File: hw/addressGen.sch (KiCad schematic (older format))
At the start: 6 parts, among them U103 74ACT283, U104 74ACT283, U105 74ACT283, U106 74ACT283, U107 74HC574, U108 74HC574

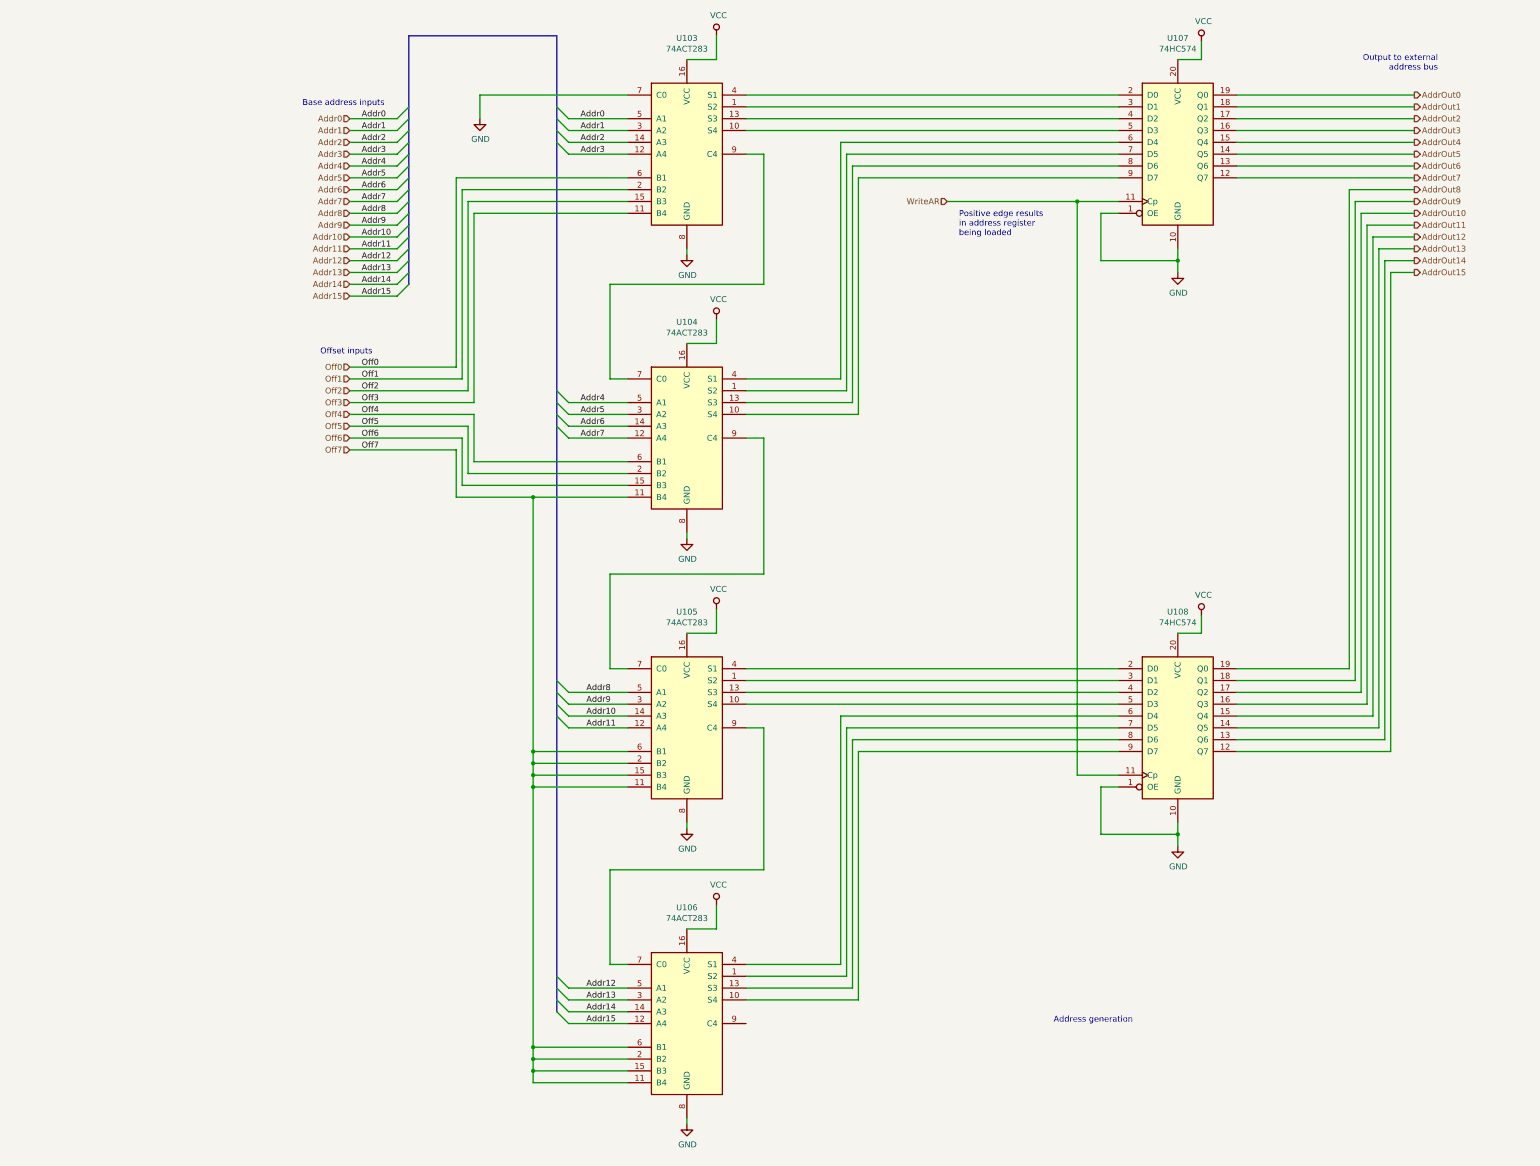
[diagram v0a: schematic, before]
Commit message: added ALo/AHi output buffers to addrGen unit
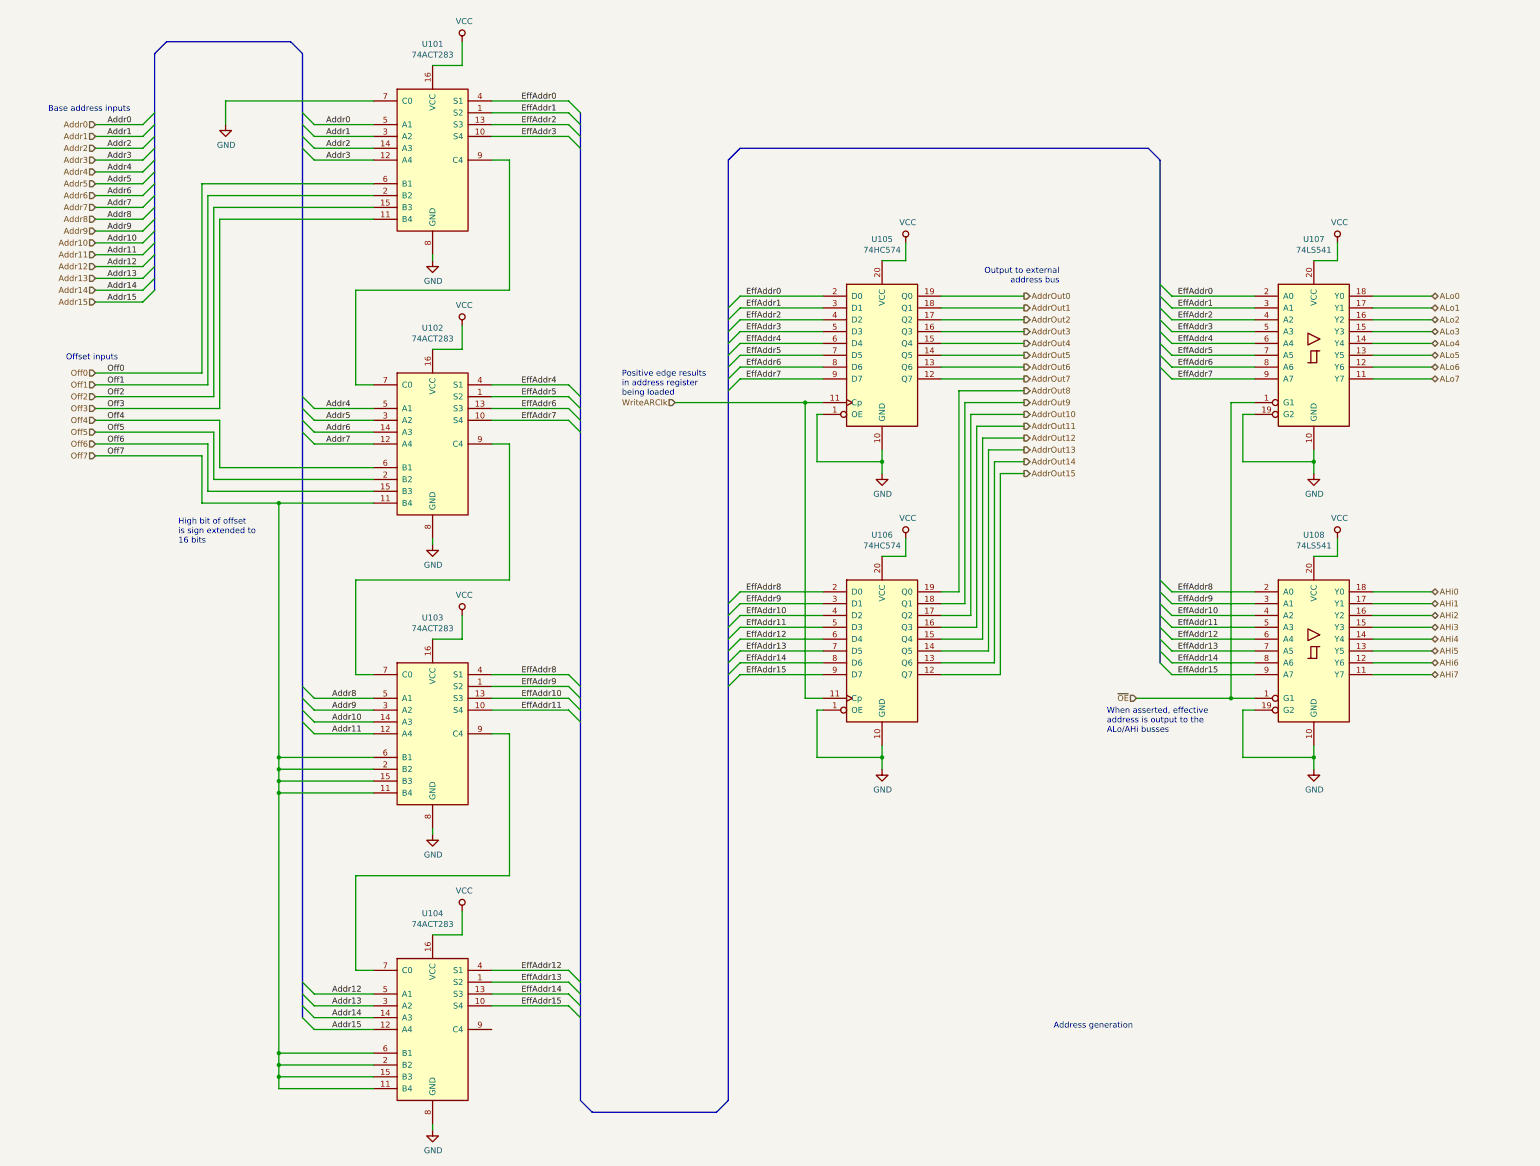
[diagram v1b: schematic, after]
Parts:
- added U107, U108: 74LS541, symbol 74xx:74LS541
- renumbered U103 to U101, U104 to U102, U105 to U103, U106 to U104, U107 to U105, U108 to U106
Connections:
- net GND: now also U107.10 (GND), U107.19 (G2), U108.10 (GND), U108.19 (G2)
- net VCC: now also U107.20 (VCC), U108.20 (VCC)
- net EffAddr1: now reaches U101.1 (S2), U105.3 (D1)
- net EffAddr1: now also U107.3 (A1)
- net EffAddr3: now reaches U101.10 (S4), U105.5 (D3)
- net EffAddr3: now also U107.5 (A3)
- net EffAddr2: now reaches U101.13 (S3), U105.4 (D2)
- net EffAddr2: now also U107.4 (A2)
- net EffAddr0: now reaches U101.4 (S1), U105.2 (D0)
- net EffAddr0: now also U107.2 (A0)
- net EffAddr5: now reaches U102.1 (S2), U105.7 (D5)
- net EffAddr5: now also U107.7 (A5)
- net EffAddr7: now reaches U102.10 (S4), U105.9 (D7)
- net EffAddr7: now also U107.9 (A7)
- net EffAddr6: now reaches U102.13 (S3), U105.8 (D6)
- net EffAddr6: now also U107.8 (A6)
- net EffAddr4: now reaches U102.4 (S1), U105.6 (D4)
- net EffAddr4: now also U107.6 (A4)
- net EffAddr9: now reaches U103.1 (S2), U106.3 (D1)
- net EffAddr9: now also U108.3 (A1)
- net EffAddr11: now reaches U103.10 (S4), U106.5 (D3)
- net EffAddr11: now also U108.5 (A3)
- net EffAddr10: now reaches U103.13 (S3), U106.4 (D2)
- net EffAddr10: now also U108.4 (A2)
- net EffAddr8: now reaches U103.4 (S1), U106.2 (D0)
- net EffAddr8: now also U108.2 (A0)
- net EffAddr13: now reaches U104.1 (S2), U106.7 (D5)
- net EffAddr13: now also U108.7 (A5)
- net EffAddr15: now reaches U104.10 (S4), U106.9 (D7)
- net EffAddr15: now also U108.9 (A7)
- net EffAddr14: now reaches U104.13 (S3), U106.8 (D6)
- net EffAddr14: now also U108.8 (A6)
- net EffAddr12: now reaches U104.4 (S1), U106.6 (D4)
- net EffAddr12: now also U108.6 (A4)
- net WriteAR renamed WriteARClk
- new net AHi0: U108.18 (Y0)
- new net AHi1: U108.17 (Y1)
- new net AHi2: U108.16 (Y2)
- new net AHi3: U108.15 (Y3)
- new net AHi4: U108.14 (Y4)
- new net AHi5: U108.13 (Y5)
- new net AHi6: U108.12 (Y6)
- new net AHi7: U108.11 (Y7)
- new net ALo0: U107.18 (Y0)
- new net ALo1: U107.17 (Y1)
- new net ALo2: U107.16 (Y2)
- new net ALo3: U107.15 (Y3)
- new net ALo4: U107.14 (Y4)
- new net ALo5: U107.13 (Y5)
- new net ALo6: U107.12 (Y6)
- new net ALo7: U107.11 (Y7)
- new net ~OE: U107.1 (G1), U108.1 (G1)
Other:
- note added: "High bit of offset\nis sign extended to\n16 bits"
- note added: "When asserted, effective\naddress is output to the\nALo/AHi busses"
- moved on the sheet: U101, U102, U103, U104, U105, U106

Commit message: generation of 0 and 1 constant offsets in addrGen
Also added pullup resistors to the offset bus to ensure
inputs are valid and also to implicitly generate the
-1 constant offset.
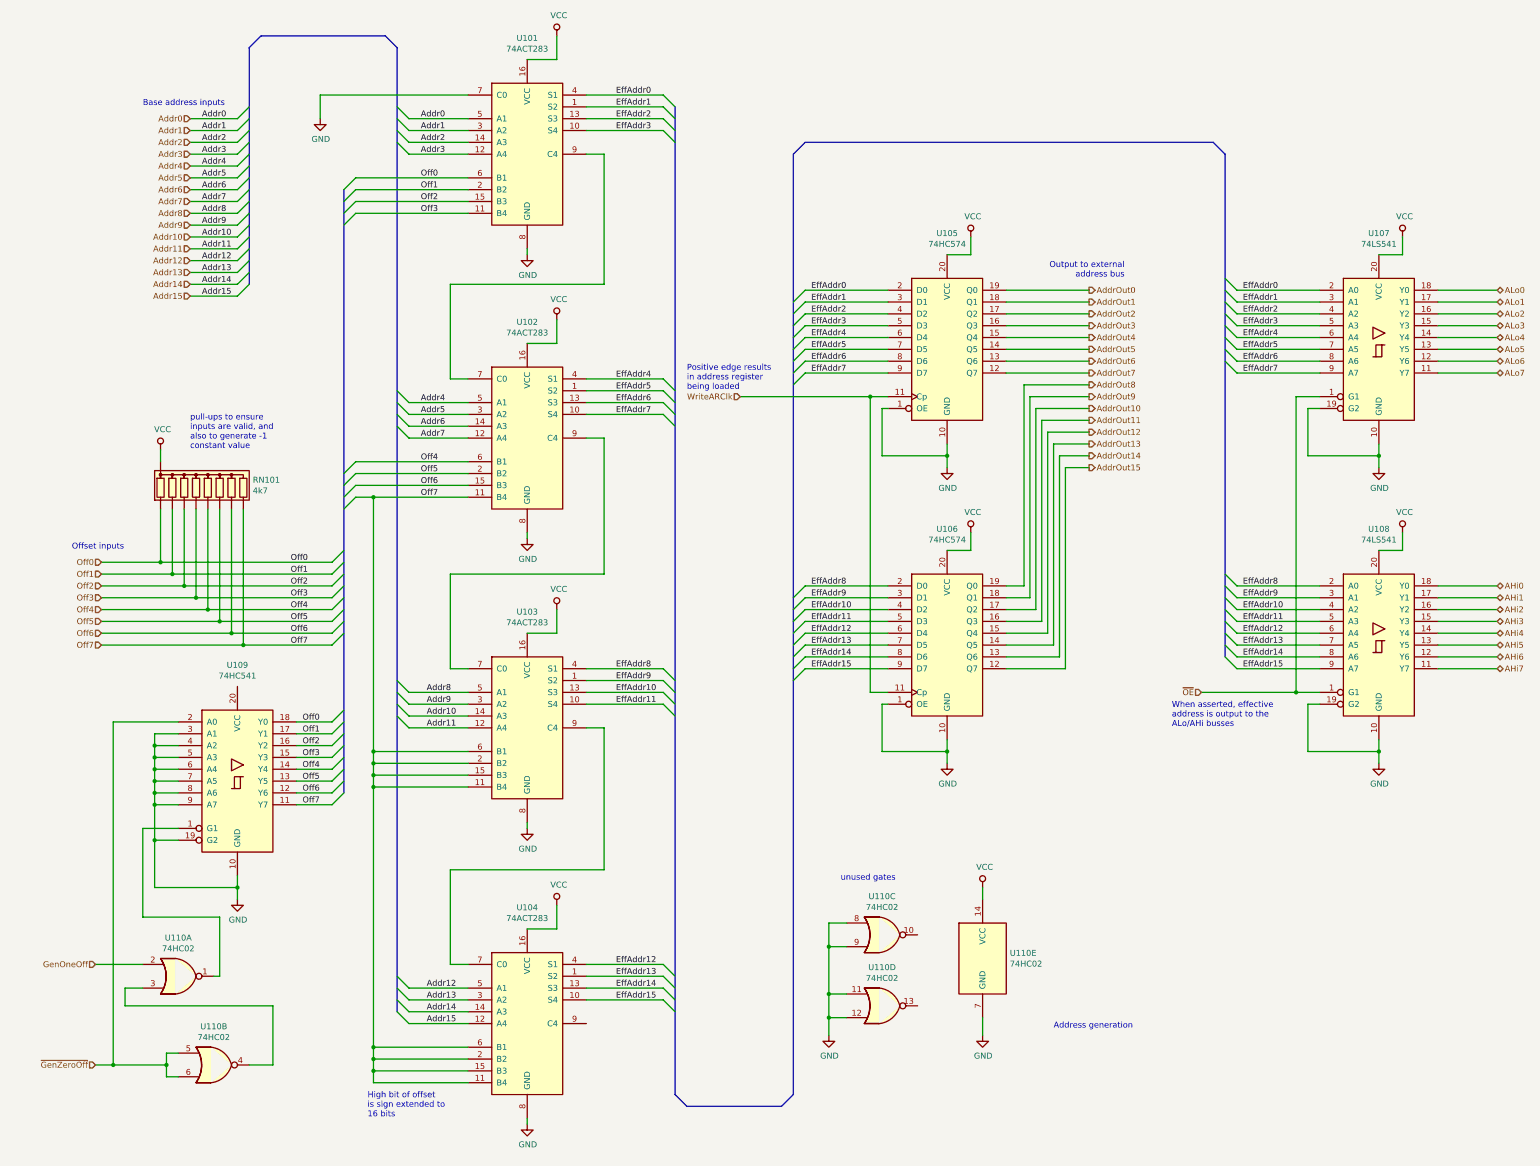
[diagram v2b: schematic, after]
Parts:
- added RN101: 4k7, Resistors_THT:R_Array_SIP9, symbol device:R_Network08
- added U109: 74HC541, symbol 74xx:74LS541
- added U110: 74HC02, symbol 74xx:74HC02
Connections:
- net GND: now also U109.10 (GND), U109.19 (G2), U109.3 (A1), U109.4 (A2), U109.5 (A3), U109.6 (A4), U109.7 (A5), U109.8 (A6), U109.9 (A7), U110.11, U110.12, U110.7 (GND), U110.8, U110.9
- net Off0: now also RN101.2 (R1), U109.18 (Y0)
- net Off1: now also RN101.3 (R2), U109.17 (Y1)
- net Off2: now also RN101.4 (R3), U109.16 (Y2)
- net Off3: now also RN101.5 (R4), U109.15 (Y3)
- net Off4: now also RN101.6 (R5), U109.14 (Y4)
- net Off5: now also RN101.7 (R6), U109.13 (Y5)
- net Off6: now also RN101.8 (R7), U109.12 (Y6)
- net Off7: now also RN101.9 (R8), U109.11 (Y7)
- net VCC: now also RN101.1 (common), U110.14 (VCC)
- new net: U109.1 (G1), U110.1
- new net: U110.3, U110.4
- new net GenOneOff: U110.2
- new net ~GenZeroOff: U109.2 (A0), U110.5, U110.6
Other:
- note added: "pull-ups to ensure\ninputs are valid, and\nalso to generate -1\nconstant value"
- note added: "unused gates"
- moved on the sheet: U101, U102, U103, U104, U105, U106, U107, U108
